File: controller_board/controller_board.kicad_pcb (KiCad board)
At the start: 2 copper layers, 62.6 x 67.2 mm, 9 parts, among them U1 NRF24L01_Breakout, U2 DEV-15583, U3 DM-OLED096-636, U4 TLV1117LV33DCYR

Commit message: adding gerber files
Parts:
- added J1: Conn_01x02_Pin, Connector_PinHeader_1.00mm:PinHeader_1x02_P1.00mm_Vertical, F.Cu at (138.3, 66.5)
- S1: value BTN_UP -> TS02-66-55-BK-100-LCR-D
- S2: value BTN_OK -> TS02-66-55-BK-100-LCR-D
- S3: value BTN DOWN -> TS02-66-55-BK-100-LCR-D
- moved U1 67.2 mm to (119.1, 122.8), turned to 180 degrees
- moved S3 39.0 mm to (106.6, 95.2), turned to 180 degrees
- moved S1 38.6 mm to (106.7, 79.2), turned to 180 degrees
- moved S2 36.9 mm to (106.8, 87.2), turned to 180 degrees
- moved U4 25.9 mm to (143.7, 72.0), turned to 0 degrees
- moved U3 24.3 mm to (149.5, 91.2), turned to 90 degrees
- moved C1 23.4 mm to (135.9, 70.5), turned to 0 degrees
- moved C2 18.1 mm to (135.8, 74.3), turned to 0 degrees
- moved U2 12.6 mm to (124.0, 87.1), turned to 0 degrees
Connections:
- C1 pad 1: Net-(U4-OUT_2) -> +3.3V
- U2 pad VIN: Net-(U4-OUT_2) -> +3.3V
- U4 pad 2: Net-(U4-OUT_2) -> +3.3V
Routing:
- net +3.3V: track 32.7 -> 76.8 mm, vias 1 -> 4
- net Net-(U1-SCK): track 0.00 -> 21.0 mm
- net Net-(U1-MISO): track 33.4 -> 12.7 mm, vias 2 -> 0
- net Net-(U1-MOSI): track 33.4 -> 18.0 mm
- net Net-(U1-~{CSN}): track 44.0 -> 29.8 mm, vias 2 -> 0
- net Net-(U1-CE): track 38.5 -> 24.5 mm, vias 3 -> 0
- net +5V: track 6.50 -> 18.4 mm
- net Net-(U4-OUT_2): track 11.0 -> 0.00 mm, vias 2 -> 0
- net Net-(U1-IRQ): track 34.5 -> 23.6 mm
- net GND: track 117.5 -> 126.7 mm, vias 8 -> 6
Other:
- board size 62.6 x 67.2 mm -> 67.2 x 62.7 mm
- board text added: "CONTROLLER BOARD"
- board text added: "NID-24"

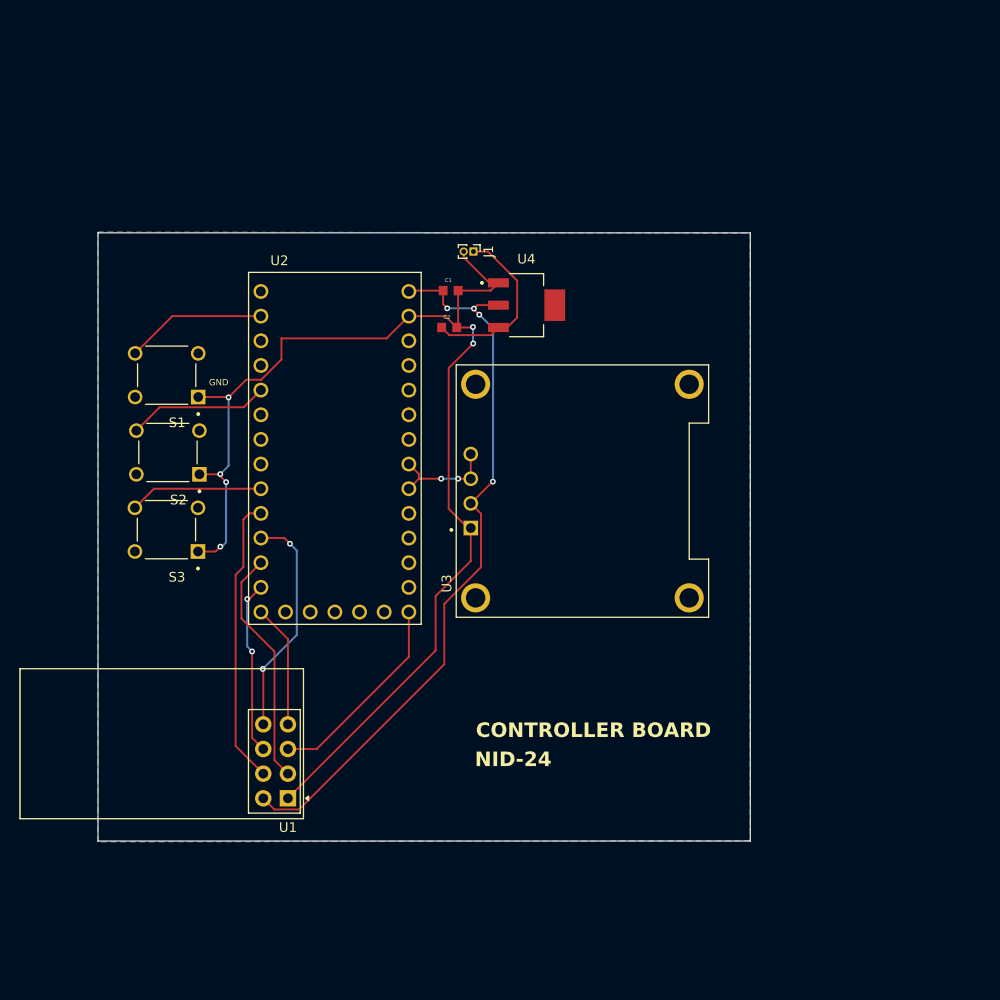
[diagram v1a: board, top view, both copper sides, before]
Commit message: added case
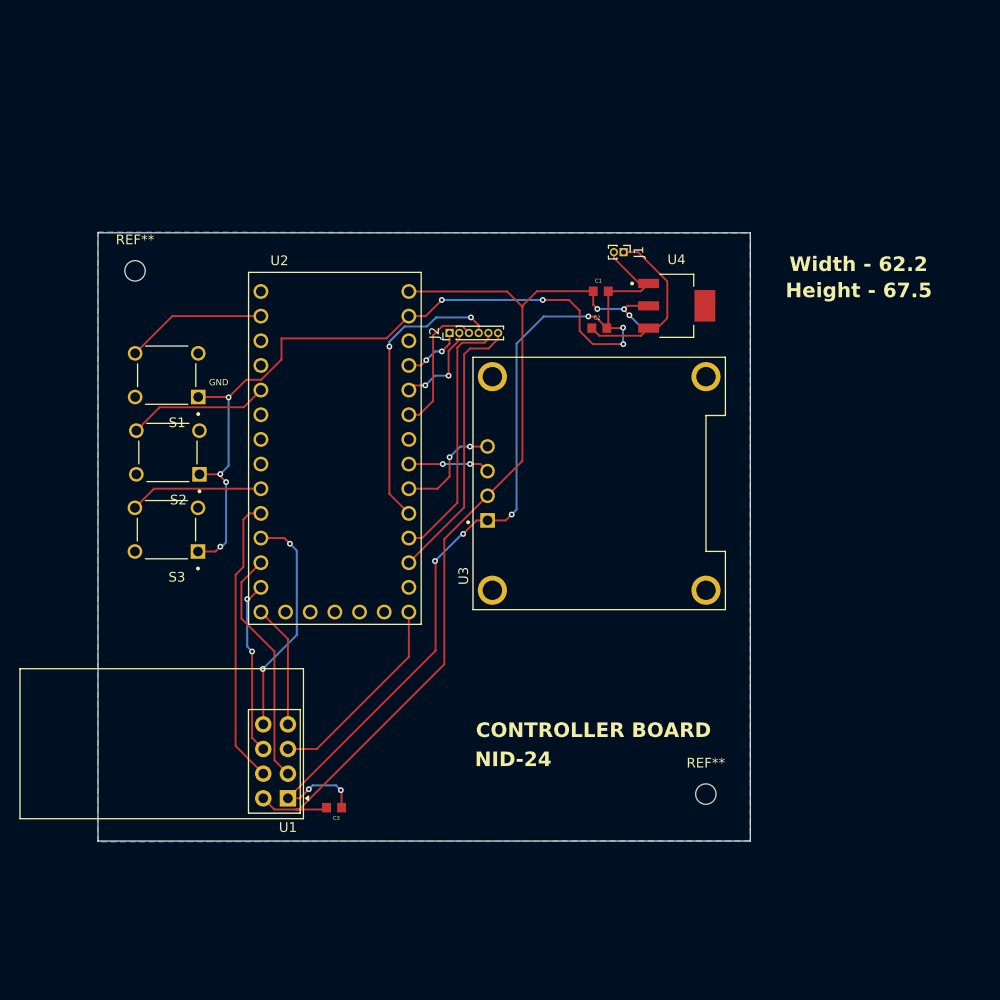
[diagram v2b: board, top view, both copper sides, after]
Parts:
- added C3: 10uF, C0603C220J5GACTU:CAPC1608X87N, F.Cu at (123.9, 123.8)
- added J2: GPIO, Connector_PinHeader_1.00mm:PinHeader_1x06_P1.00mm_Vertical, F.Cu at (135.8, 74.9)
- added REF**: MountingHole_2.1mm, MountingHole:MountingHole_2.1mm, F.Cu at (162.2, 122.4)
- added REF**: MountingHole_2.1mm, MountingHole:MountingHole_2.1mm, F.Cu at (103.4, 68.5)
- C1: footprint C0603C223J5RACTU:CAPC1608X87N -> C0603C220J5GACTU:CAPC1608X87N
- moved C1 15.5 mm to (151.4, 70.6)
- moved C2 15.5 mm to (151.2, 74.4)
- moved J1 15.5 mm to (153.7, 66.6)
- moved U4 15.5 mm to (159.2, 72.1)
- moved U3 1.90 mm to (151.2, 90.4)
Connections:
- U2 pad 15: unconnected-(U2-Pad15) -> GPIO 15
- U2 pad 16: unconnected-(U2-Pad16) -> GPIO 16
- U2 pad 17: unconnected-(U2-Pad17) -> GPIO 17
- U2 pad 18: Net-(U3-SCL) -> GPIO 18
- U2 pad 19: Net-(U3-SCL) -> GPIO 19
- U2 pad 21: unconnected-(U2-Pad21) -> GPIO 21
- U2 pad 22: unconnected-(U2-Pad22) -> GPIO 22
- U2 pad 23: unconnected-(U2-Pad23) -> GPIO 23
- U3 pad 3: Net-(U3-SCL) -> GPIO 19
- U3 pad 4: Net-(U3-SCL) -> GPIO 18
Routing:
- net GND: track 126.7 -> 167.8 mm, vias 6 -> 14
- net GPIO 17: track 0.00 -> 30.0 mm, vias 0 -> 2
- net GPIO 15: track 0.00 -> 28.6 mm
- net GPIO 16: track 0.00 -> 26.7 mm
- net +3.3V: track 76.8 -> 99.5 mm, vias 4 -> 3
- net GPIO 21: track 0.00 -> 14.3 mm
- net Net-(U3-SCL): track 11.3 -> 0.00 mm, vias 2 -> 0
- net GPIO 18: track 0.00 -> 11.1 mm, vias 0 -> 2
- net GPIO 22: track 0.00 -> 9.57 mm, vias 0 -> 2
- net GPIO 19: track 0.00 -> 8.41 mm, vias 0 -> 2
- net GPIO 23: track 0.00 -> 6.22 mm, vias 0 -> 2
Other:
- board text added: "Height - 67.5"
- board text added: "Width - 62.2"

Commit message: added case and new images of ADS1293 breakout board and controller board case
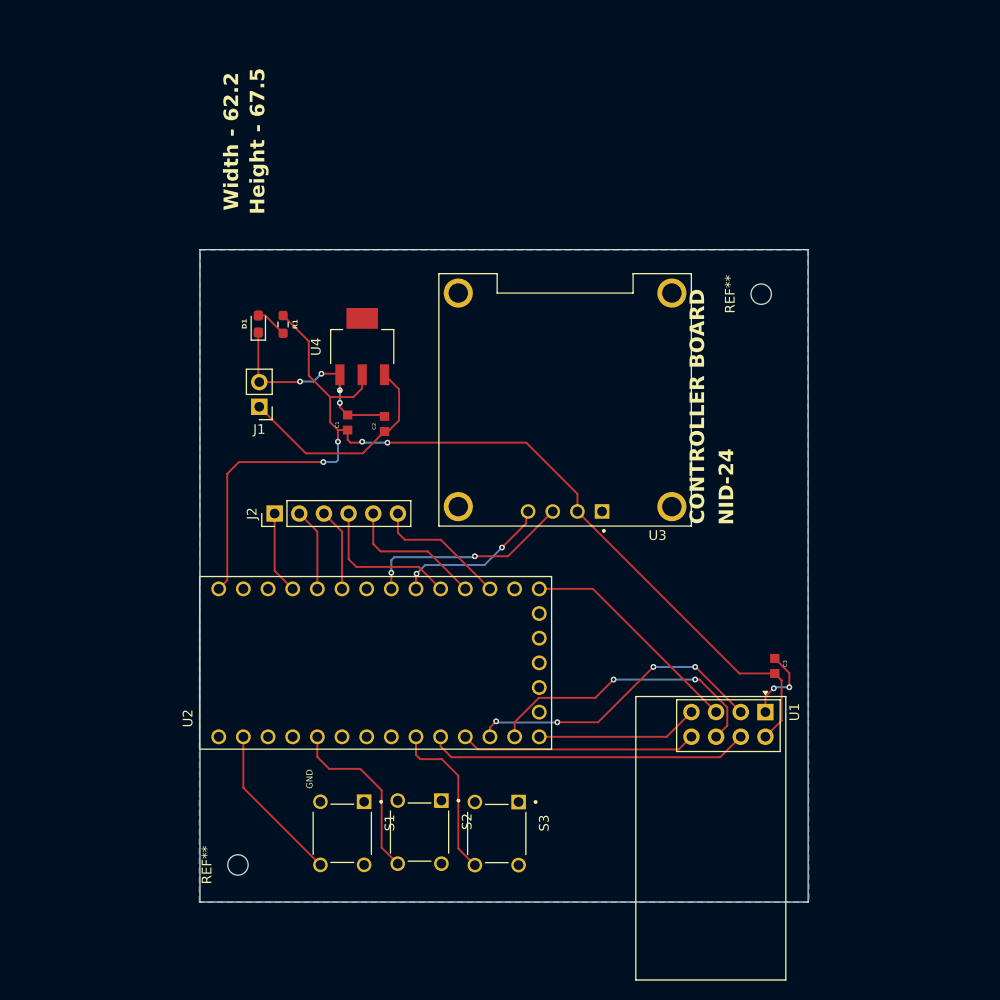
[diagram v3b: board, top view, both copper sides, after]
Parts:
- added D1: LED, LED_SMD:LED_0603_1608Metric_Pad1.05x0.95mm_HandSolder, F.Cu at (116.1, 74.0)
- added R1: 220 Ohms, Resistor_SMD:R_0603_1608Metric_Pad0.98x0.95mm_HandSolder, F.Cu at (118.7, 74.0)
- J1: footprint Connector_PinHeader_1.00mm:PinHeader_1x02_P1.00mm_Vertical -> Connector_PinHeader_2.54mm:PinHeader_1x02_P2.54mm_Vertical
- J2: footprint Connector_PinHeader_1.00mm:PinHeader_1x06_P1.00mm_Vertical -> Connector_PinHeader_2.54mm:PinHeader_1x06_P2.54mm_Vertical
- moved REF** 62.1 mm to (114.0, 129.7), turned to 90 degrees
- moved REF** 51.8 mm to (167.9, 70.9), turned to 90 degrees
- moved S1 50.5 mm to (124.7, 126.4), turned to -90 degrees
- moved U1 50.0 mm to (168.3, 114.0), turned to -90 degrees
- moved C3 47.7 mm to (169.3, 109.2), turned to -90 degrees
- moved S2 46.9 mm to (132.7, 126.3), turned to -90 degrees
- moved S3 46.2 mm to (140.7, 126.5), turned to -90 degrees
- moved J1 40.8 mm to (116.2, 82.5), turned to 180 degrees
- moved U4 32.7 mm to (126.8, 76.3), turned to 90 degrees
- moved C1 29.4 mm to (125.3, 84.1), turned to 90 degrees
- moved J2 25.9 mm to (117.8, 93.5)
- moved C2 24.2 mm to (129.1, 84.3), turned to 90 degrees
- moved U2 22.2 mm to (128.5, 108.9), turned to 90 degrees
- moved U3 9.30 mm to (147.7, 81.8), turned to 180 degrees
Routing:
- net GND: track 167.8 -> 30.2 mm, vias 14 -> 6
- net GPIO 15: track 28.6 -> 13.9 mm
- net GPIO 17: track 30.0 -> 15.4 mm, vias 2 -> 0
- net GPIO 19: track 8.41 -> 21.7 mm
- net GPIO 16: track 26.7 -> 14.5 mm
- net Net-(U1-MOSI): track 18.0 -> 29.9 mm
- net +3.3V: track 99.5 -> 111.1 mm, vias 3 -> 4
- net Net-(U1-CE): track 24.5 -> 31.4 mm, vias 0 -> 4
- net GPIO 21: track 14.3 -> 8.53 mm
- net GPIO 18: track 11.1 -> 16.3 mm
- net +5V: track 18.4 -> 23.1 mm
- net Net-(U1-MISO): track 12.7 -> 16.7 mm
- net GPIO 3: track 14.6 -> 18.4 mm
- net Net-(U1-~{CSN}): track 29.8 -> 33.2 mm
- net Net-(D1-A): track 0.00 -> 3.31 mm
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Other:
- board size 67.2 x 62.7 mm -> 62.7 x 67.2 mm
